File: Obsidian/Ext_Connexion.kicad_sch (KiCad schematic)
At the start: 36 parts, among them J4 Conn_02x20_Odd_Even

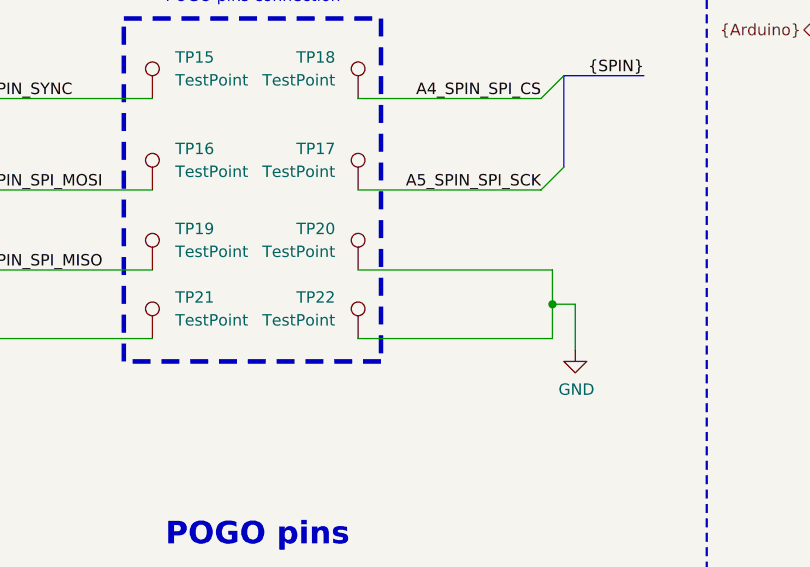
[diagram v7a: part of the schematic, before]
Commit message: Adding the gnd shield
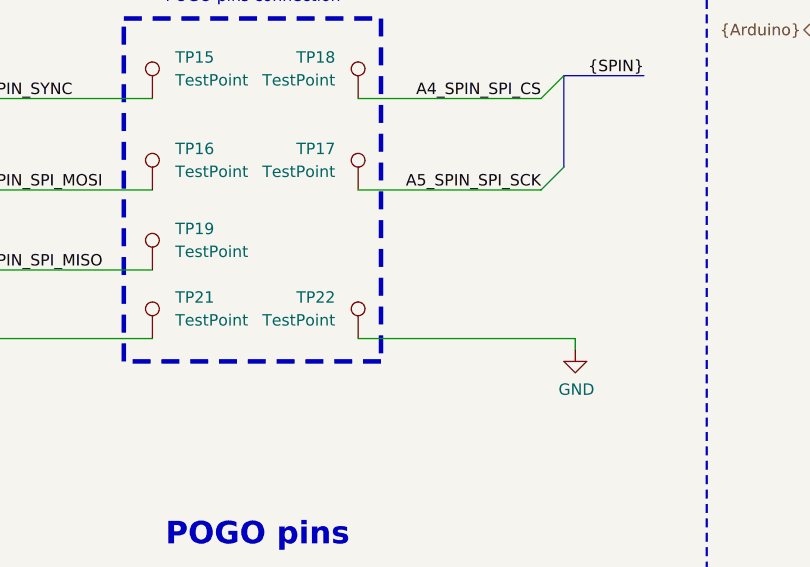
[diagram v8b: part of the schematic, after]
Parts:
- removed TP20: TestPoint, Footprint:TestPoint_Pad_D2.0mm, symbol Connector:TestPoint
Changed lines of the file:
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@@
-	)
-	(junction
-		(at 99.06 67.31)
-		(diameter 0)
-		(color 0 0 0 0)
 	)
 	(junction
@@
 	(wire
 		(pts
-			(xy 99.06 63.5) (xy 99.06 67.31)
-		)
-		(stroke
-			(width 0)
-			(type default)
-		)
-	)
-	(wire
-		(pts
 			(xy 58.42 140.97) (xy 22.86 140.97)
 		)
@@
 	(wire
 		(pts
-			(xy 101.6 67.31) (xy 99.06 67.31)
-		)
-		(stroke
-			(width 0)
-			(type default)
-		)
-	)
-	(wire
-		(pts
 			(xy 255.27 44.45) (xy 270.51 44.45)
 		)
@@
 		(pts
 			(xy 142.24 44.45) (xy 160.02 44.45)
-		)
-		(stroke
-			(width 0)
-			(type default)
-		)
-	)
-	(wire
-		(pts
-			(xy 99.06 67.31) (xy 99.06 71.12)
 		)
 		(stroke
@@
 	(wire
 		(pts
-			(xy 77.47 71.12) (xy 99.06 71.12)
-		)
-		(stroke
-			(width 0)
-			(type default)
-		)
-	)
-	(wire
-		(pts
-			(xy 101.6 72.39) (xy 101.6 67.31)
+			(xy 77.47 71.12) (xy 101.6 71.12)
+		)
+		(stroke
+			(width 0)
+			(type default)
+		)
+	)
+	(wire
+		(pts
+			(xy 101.6 72.39) (xy 101.6 71.12)
 		)
 		(stroke
@@
 		(pts
 			(xy 91.44 163.83) (xy 71.12 163.83)
-		)
-		(stroke
-			(width 0)
-			(type default)
-		)
-	)
-	(wire
-		(pts
-			(xy 77.47 63.5) (xy 99.06 63.5)
 		)
 		(stroke
@@
 					(unit 1)
 				)
-			)
-		)
-	)
-	(symbol
-		(lib_id "Connector:TestPoint")
-		(at 77.47 63.5 0)
-		(mirror y)
-		(unit 1)
-		(exclude_from_sim no)
-		(in_bom yes)
-		(on_board yes)
-		(dnp no)
-		(fields_autoplaced yes)
-		(property "Reference" "TP20"
-			(at 74.93 58.9279 0)
-			(effects
-				(font
-					(size 1.27 1.27)
-				)
-				(justify left)
-			)
-		)
-		(property "Value" "TestPoint"
-			(at 74.93 61.4679 0)
-			(effects
-				(font
-					(size 1.27 1.27)
-				)
-				(justify left)
-			)
-		)
-		(property "Footprint" "Footprint:TestPoint_Pad_D2.0mm"
-			(at 72.39 63.5 0)
-			(effects
-				(font
-					(size 1.27 1.27)
-				)
-				(hide yes)
-			)
-		)
-		(property "Datasheet" "~"
-			(at 72.39 63.5 0)
-			(effects
-				(font
-					(size 1.27 1.27)
-				)
-				(hide yes)
-			)
-		)
-		(property "Description" "test point"
-			(at 77.47 63.5 0)
-			(effects
-				(font
-					(size 1.27 1.27)
-				)
-				(hide yes)
-			)
-		)
-		(pin "1"
-		)
-		(instances
-			(project "Obsidian"
-				(path "/c2a4f786-b14c-434a-acf7-b20fb2221b0b/37c76a7d-e360-409e-9f8e-819f870af943"
-					(reference "TP20")
-					(unit 1)
-				)
